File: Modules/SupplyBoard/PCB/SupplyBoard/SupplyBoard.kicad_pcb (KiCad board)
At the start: 2 copper layers, 46.6 x 57 mm, 86 parts, among them J1 CI_BATT, J2 SW-DP, J3 CIO_MAIN_CONNECTOR, Q1 AGP30P35AP, Q2 IRLM2502, SW1 RESET, SW2 SW_SPDT_312, U1 STM32L031G6Ux, U2 TPS63070, U6 TMP20AIDCK

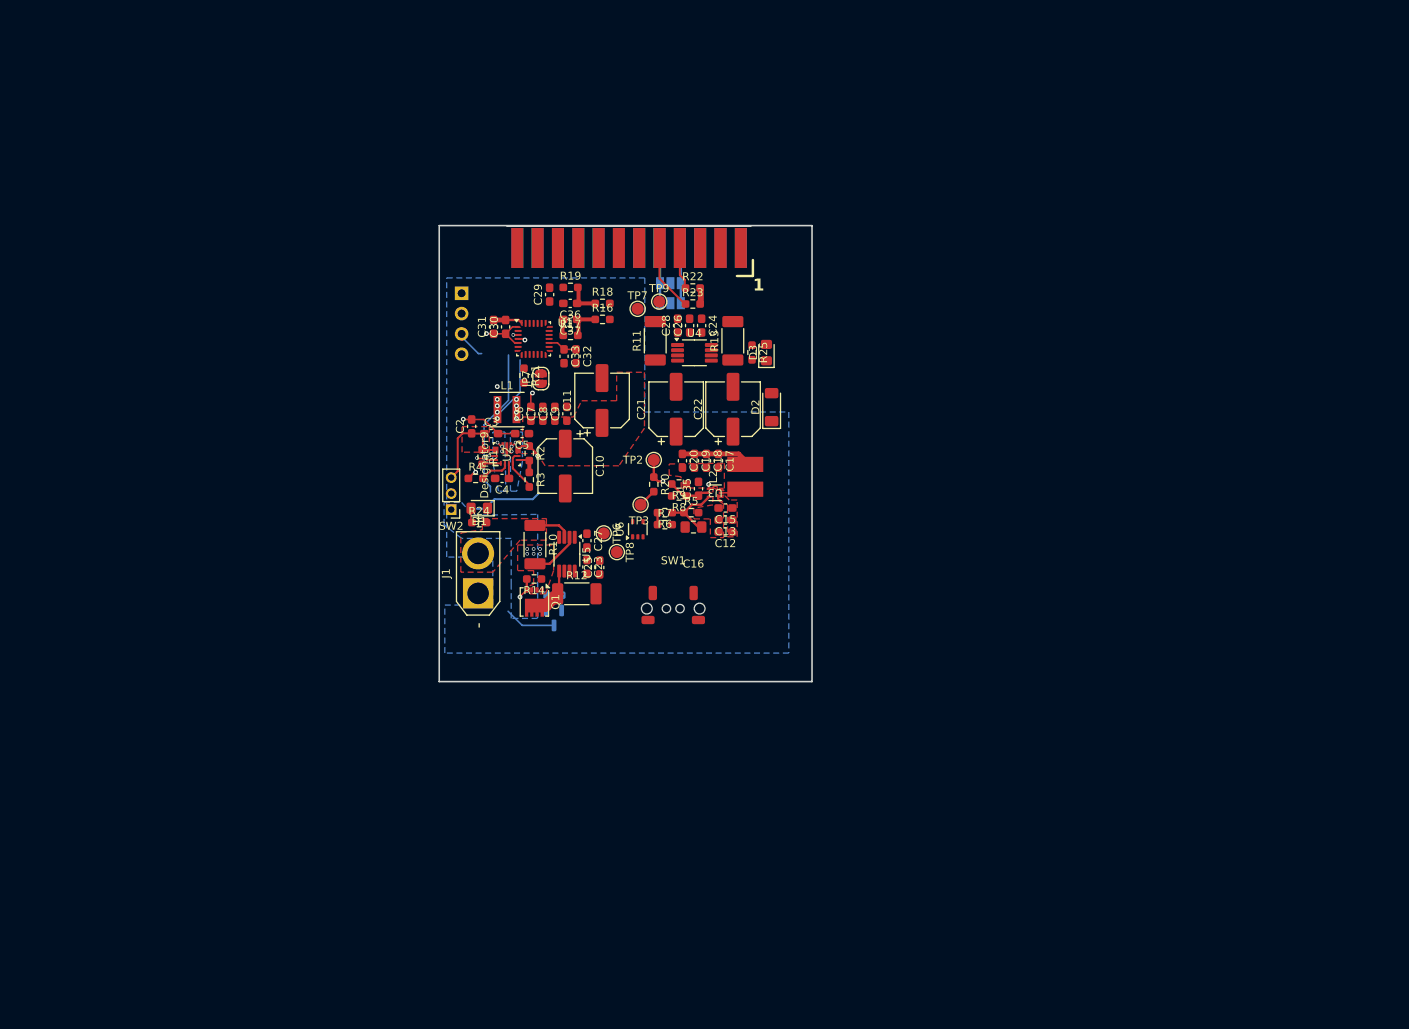
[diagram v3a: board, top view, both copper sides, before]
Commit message: Updated supply board for v2, and BMP280 tinkering project
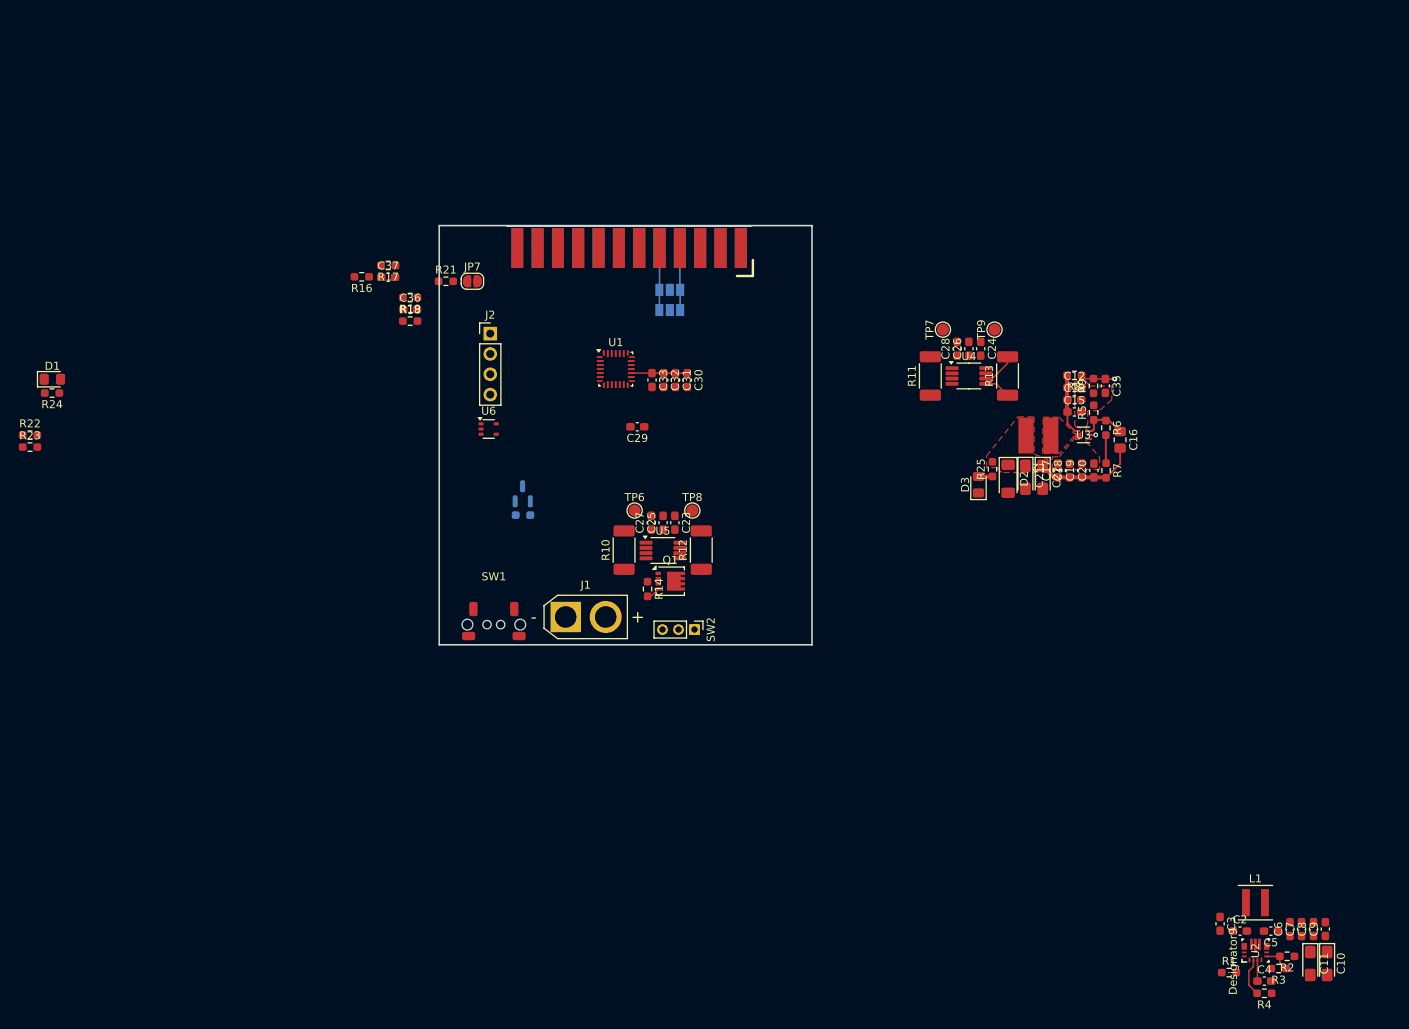
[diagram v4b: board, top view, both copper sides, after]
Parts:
- removed R20: 10k, Resistor_SMD:R_0603_1608Metric_Pad0.98x0.95mm_HandSolder
- removed TP2: 3v3_PG, TestPoint:TestPoint_Pad_D1.5mm
- removed TP3: 3v3_PG_VCC, TestPoint:TestPoint_Pad_D1.5mm
- C10, C11, C21, C22: footprint Capacitor_SMD:CP_Elec_6.3x5.4 -> Capacitor_Tantalum_SMD:CP_EIA-3216-18_Kemet-A_Pad1.58x1.35mm_HandSolder
- J2: moved to F.Cu
- moved R4 117.7 mm to (196.4, 143.7), turned to 180 degrees
- moved C2 114.9 mm to (193.4, 135.9), turned to 0 degrees
- moved C6 114.7 mm to (199.6, 135.6)
- moved C7 114.6 mm to (201.1, 135.6)
- moved C8 114.6 mm to (202.6, 135.6)
- moved C9 114.6 mm to (204.1, 135.6)
- moved C4 114.1 mm to (196.4, 142.1), turned to 0 degrees
- moved C10 113.7 mm to (204.3, 139.9)
- moved R2 113.7 mm to (199.3, 139.0), turned to 180 degrees
- moved R1 113.5 mm to (192.0, 141.1), turned to 0 degrees
- moved C11 113.1 mm to (202.2, 139.9), turned to -90 degrees
- moved C5 112.4 mm to (197.3, 135.9)
- moved U2 112.3 mm to (195.3, 138.3)
- moved L1 112.0 mm to (195.3, 132.3)
- moved R3 111.8 mm to (198.2, 140.6), turned to 180 degrees
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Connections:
- C23 pad 2: +3V3 -> +3.3V
- C24 pad 2: +3V3 -> +3.3V
- U3 pad 4: Net-(U3-PG) -> unconnected-(U3-PG-Pad4)
- U4 pad 8: +3V3 -> +3.3V
- U5 pad 8: +3V3 -> +3.3V
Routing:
- net GND: track 22.1 -> 0.00 mm, vias 3 -> 0
- net /Controlador/5V_ENABLE: track 20.2 -> 0.00 mm, vias 2 -> 0
- net /LIPO_TO_5V/5V_OUT: track 13.2 -> 0.00 mm, vias 2 -> 0
- net /Controlador/~{RESET}: track 9.93 -> 0.00 mm, vias 2 -> 0
- net /I2C0_SCL: track 8.31 -> 0.00 mm
- net /LIPO_TO_3V/3V3_OUT: track 8.44 -> 16.3 mm
- net Net-(Q1-G): track 9.09 -> 1.71 mm, vias 1 -> 0
- net /BATT_BYPASS_SW/BATT_OUT: track 6.43 -> 0.00 mm
- net /BATT_INPUT: track 6.17 -> 0.00 mm, vias 6 -> 0
- net /I2C0_SDA: track 5.26 -> 0.00 mm
- net /CurrentSense_Lipo/V_IN_{1}: track 4.77 -> 0.00 mm
- net /Controlador/BATT_INPUT: track 12.4 -> 7.70 mm
- net Net-(U3-PG): track 4.08 -> 0.00 mm, vias 2 -> 0
- net /Controlador/V_{IN}_SENSE: track 4.00 -> 0.00 mm
- net /Controlador/V_{5V}_SENSE: track 3.93 -> 0.00 mm
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- added copper zone on F.Cu, net /LIPO_TO_3V/3V3_OUT
- added copper zone on F.Cu, net Net-(L2-+)
- removed copper zone on B.Cu, net /BATT_INPUT
- removed copper zone on F.Cu, net /BATT_INPUT
- removed copper zone on F.Cu, net /CurrentSense_Lipo/V_IN_{1}
- removed copper zone on F.Cu, net /LIPO_TO_5V/5V_OUT
- removed copper zone on B.Cu, net GND
- removed copper zone on B.Cu, net Net-(L1-+)
- removed copper zone on B.Cu, net Net-(L1--)
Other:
- board size 46.6 x 57 mm -> 46.6 x 52.4 mm

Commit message: Muchas cosas: Backplane, SupplyBoard y principio SensorBoard
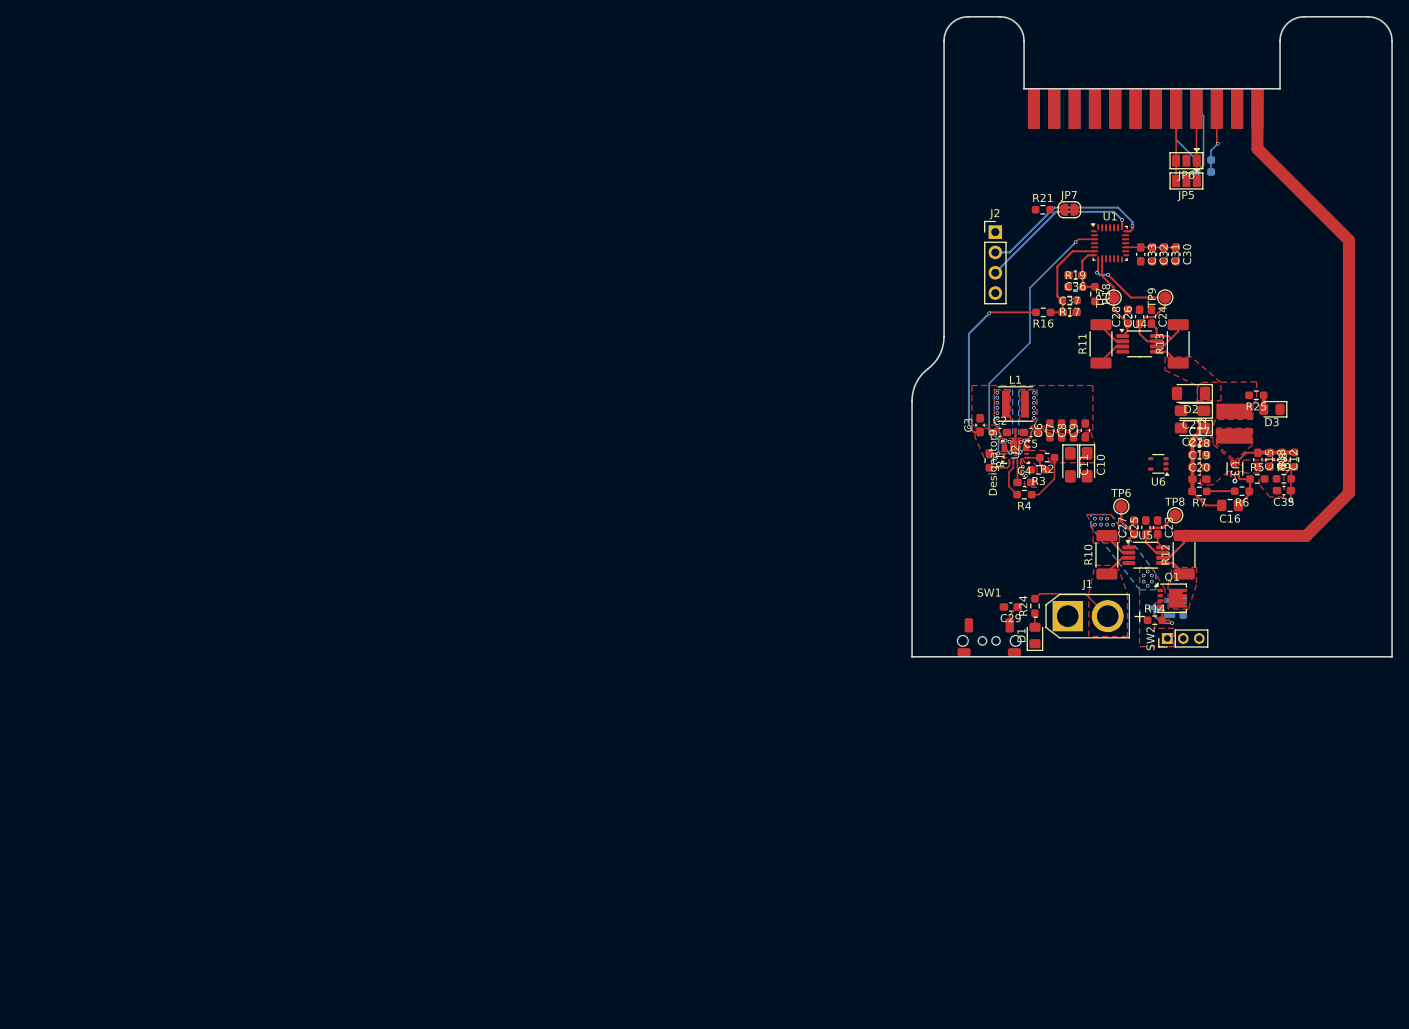
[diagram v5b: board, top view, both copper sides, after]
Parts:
- J3, R22, R23: moved to B.Cu
- JP5, JP6: moved to F.Cu
- moved R23 151.1 mm to (188.9, 39.5)
- moved R22 150.4 mm to (188.9, 41.0)
- moved D1 126.9 mm to (167.8, 98.9), turned to 90 degrees
- moved R24 125.7 mm to (167.8, 95.2), turned to 90 degrees
- moved R18 85.7 mm to (175.3, 56.3), turned to -90 degrees
- moved R16 85.3 mm to (168.8, 58.5)
- moved C37 85.3 mm to (172.1, 58.5)
- moved R17 85.3 mm to (172.1, 57.1)
- moved U6 83.8 mm to (183.2, 77.5), turned to 180 degrees
- moved R15 83.3 mm to (186.3, 95.5), turned to -90 degrees
- moved C36 83.3 mm to (172.8, 53.9), turned to 180 degrees
- moved R19 83.2 mm to (172.8, 55.4), turned to 0 degrees
- moved Q2 81.2 mm to (183.6, 95.5), turned to 180 degrees
- moved JP7 75.2 mm to (172.1, 45.7)
- moved R21 75.2 mm to (168.8, 45.7)
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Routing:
- net /BATT_BYPASS: track 0.00 -> 80.0 mm
- net /Controlador/5V_ENABLE: track 0.00 -> 34.6 mm, vias 0 -> 2
- net /Controlador/BATT_INPUT: track 7.70 -> 30.6 mm, vias 0 -> 2
- net /Controlador/SWDIO: track 0.00 -> 22.0 mm, vias 0 -> 1
- net /I_{3v3}_SENSE: track 0.00 -> 20.5 mm, vias 0 -> 2
- net /Controlador/SWCLK: track 0.00 -> 20.4 mm, vias 0 -> 1
- net /CurrentSense_Lipo/V_IN_{1}: track 0.00 -> 14.3 mm
- net +3.3V: track 11.3 -> 24.6 mm, vias 0 -> 1
- net /Controlador/V_{IN}_SENSE: track 0.00 -> 13.0 mm
- net /I_{5v}_SENSE: track 0.00 -> 11.3 mm
- net /LIPO_TO_5V/5V_OUT: track 0.00 -> 9.98 mm
- net /I2C0_SDA: track 0.00 -> 8.63 mm
- net /I_{BYPASS}_SENSE: track 0.00 -> 8.27 mm
- net /I2C0_SCL: track 0.00 -> 7.45 mm
- net /Controlador/V_{5V}_SENSE: track 0.00 -> 6.58 mm
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- added copper zone on F.Cu, net /BATT_BYPASS_SW/BATT_OUT
- added copper zone on B.Cu, net /BATT_INPUT
- added copper zone on F.Cu, net /BATT_INPUT
- added copper zone on F.Cu, net /Controlador/BATT_INPUT
- added copper zone on F.Cu, net /CurrentSense_Lipo/V_IN_{1}
- added copper zone on F.Cu, net /LIPO_TO_5V/5V_OUT
- added copper zone on B.Cu, net Net-(L1-+)
- added copper zone on F.Cu, net Net-(L1-+)
- added copper zone on B.Cu, net Net-(L1--)
- added copper zone on F.Cu, net Net-(L1--)
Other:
- board size 46.6 x 52.4 mm -> 60 x 80 mm

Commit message: Finished Supply board
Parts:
- added G***: LOGO, IcaroFootprints:LogoGluon_12mm, B.Cu at (158.8, 92.7)
- added REF**: MountingHole_3.2mm_M3_DIN965, MountingHole:MountingHole_3.2mm_M3_DIN965, F.Cu at (197.6, 46.2)
- added REF**: MountingHole_3.2mm_M3_DIN965, MountingHole:MountingHole_3.2mm_M3_DIN965, F.Cu at (197.4, 96.6)
- added REF**: KiCad-Logo2_5mm_SilkScreen, Symbol:KiCad-Logo2_5mm_SilkScreen, B.Cu at (197.5, 57.8)
- added TP1: STM_SPEED, TestPoint:TestPoint_Pad_D1.5mm, F.Cu at (174.9, 64.8)
- added kibuzzard-67BD8B4D: G***, kibuzzard-67BD8B4D, F.Cu at (174.0, 61.3)
- added kibuzzard-67BD8B63: G***, kibuzzard-67BD8B63, F.Cu at (174.0, 62.9)
- added kibuzzard-67BD8B96: G***, kibuzzard-67BD8B96, F.Cu at (186.3, 57.3)
- added kibuzzard-67BD8B9D: G***, kibuzzard-67BD8B9D, F.Cu at (191.4, 58.2)
- added kibuzzard-67BD8B9D: G***, kibuzzard-67BD8B9D, B.Cu at (191.4, 60.0)
- added kibuzzard-67BD8BAB: G***, kibuzzard-67BD8BAB, F.Cu at (188.8, 57.3)
- added kibuzzard-67BD8BAB: G***, kibuzzard-67BD8BAB, F.Cu at (173.6, 57.4)
- added kibuzzard-67BD8C21: G***, kibuzzard-67BD8C21, B.Cu at (186.3, 57.0)
- added kibuzzard-67BD8C4F: G***, kibuzzard-67BD8C4F, B.Cu at (173.6, 57.3)
- added kibuzzard-67BD8C4F: G***, kibuzzard-67BD8C4F, B.Cu at (188.8, 57.3)
- added kibuzzard-67BD8C4F: G***, kibuzzard-67BD8C4F, B.Cu at (166.0, 57.2)
- added kibuzzard-67BD8EAE: G***, kibuzzard-67BD8EAE, F.Cu at (173.6, 82.8)
- added kibuzzard-67BD8EBE: G***, kibuzzard-67BD8EBE, F.Cu at (174.2, 80.3)
- added kibuzzard-67BD8ECC: G***, kibuzzard-67BD8ECC, F.Cu at (185.9, 66.5)
- added kibuzzard-67BD8EE5: G***, kibuzzard-67BD8EE5, F.Cu at (197.6, 66.9)
- added kibuzzard-67BD90D0: G***, kibuzzard-67BD90D0, F.Cu at (163.2, 69.6)
- added kibuzzard-67BD90D4: G***, kibuzzard-67BD90D4, F.Cu at (163.2, 72.1)
- added kibuzzard-67BD90DE: G***, kibuzzard-67BD90DE, F.Cu at (162.3, 67.1)
- added kibuzzard-67BD90E3: G***, kibuzzard-67BD90E3, F.Cu at (162.6, 74.7)
- added kibuzzard-67BD93F4: G***, kibuzzard-67BD93F4, B.Cu at (185.1, 63.7)
- added kibuzzard-67BDA321: G***, kibuzzard-67BDA321, F.Cu at (178.1, 64.8)
- C10, C11: footprint Capacitor_Tantalum_SMD:CP_EIA-3216-18_Kemet-A_Pad1.58x1.35mm_HandSolder -> Capacitor_Tantalum_SMD:CP_EIA-3528-21_Kemet-B_Pad1.50x2.35mm_HandSolder
- L1: footprint Inductor_SMD:L_Coilcraft_XxL4040 -> Inductor_SMD:L_Cenker_CKCS4030
- moved J3 20.8 mm to (177.4, 53.5)
- moved R18 20.6 mm to (170.2, 76.2)
- moved JP5 20.4 mm to (181.7, 61.9)
- moved JP6 20.1 mm to (181.7, 59.1)
- moved U1 20.1 mm to (172.1, 69.4)
- moved JP7 19.9 mm to (164.5, 64.2)
- moved R21 19.9 mm to (161.2, 64.2)
- moved C30 19.9 mm to (181.4, 70.8)
- moved C31 19.9 mm to (179.9, 70.8)
- moved C32 19.9 mm to (178.4, 70.8)
- moved C33 19.9 mm to (176.9, 70.8)
- moved R22 19.5 mm to (184.3, 59.9)
- moved R23 19.5 mm to (184.3, 58.4)
- moved C37 19.4 mm to (166.0, 77.0)
- moved R16 19.4 mm to (162.7, 77.0)
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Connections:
- U1 pad 14: /SPI.MOSI -> /SPI.MISO
- U1 pad 15: /SPI.MISO -> /SPI.MOSI
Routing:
- net GND: track 2.26 -> 91.5 mm, vias 3 -> 72
- net +3.3V: track 24.6 -> 101.1 mm, vias 1 -> 3
- net /Controlador/BATT_INPUT: track 30.6 -> 73.9 mm, vias 2 -> 24
- net +5V: track 3.67 -> 40.8 mm, vias 0 -> 3
- net /BYPASS_EN: track 1.73 -> 38.4 mm, vias 0 -> 1
- net /Controlador/~{RESET}: track 2.70 -> 32.2 mm, vias 0 -> 2
- net /SPI.CS0: track 0.00 -> 29.2 mm, vias 0 -> 2
- net /SPI.CS1: track 0.00 -> 26.8 mm, vias 0 -> 1
- net /SPI.MISO: track 0.00 -> 25.0 mm, vias 0 -> 2
- net /SPI.MOSI: track 0.00 -> 22.9 mm, vias 0 -> 2
- net /I_{3v3}_SENSE: track 20.5 -> 40.9 mm
- net /I_{5v}_SENSE: track 11.3 -> 31.6 mm, vias 0 -> 2
- net /SPI.SCK: track 0.00 -> 19.2 mm, vias 0 -> 2
- net /LIPO_TO_5V/5V_OUT: track 9.98 -> 28.9 mm, vias 0 -> 6
- net /I_{BYPASS}_SENSE: track 8.27 -> 26.7 mm
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- added copper zone on F.Cu, net /BATT_BYPASS
- added copper zone on B.Cu, net /Controlador/BATT_INPUT
- added copper zone on B.Cu, net GND
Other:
- board size 60 x 80 mm -> 50 x 60 mm
- board text added: "C17-20"
- board text added: "C30-33"
- board text added: "C6-C9"
- board text added: "Gracias a todos:"
- board text added: "Proyecto Ícaro SupplyBoard V1.0 by: @labgluon"
- board text added: "gordon_clark movich4 adiiran pulwef kerneltron victor_gomezzz dhontecillas pintzio2 bark12 alnaumiwebs"
- board text added: "laboratoriocautin qvision_dev tuboniatofugaz t3l3mac0 rafaromevi hec100h diegomallo jsochoa crovodovod joseju_ch"
- board text added: "spuertes araba_st zurano_ carlosbetdev gorn6_ david_wiki sergivv txusev enlopa blacai"
